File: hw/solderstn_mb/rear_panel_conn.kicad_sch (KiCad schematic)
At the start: 44 parts, among them J1001 SJ-3571N, J1002 Conn_WR-FAST_01x03, J1003 Conn_WR-FAST_01x03, J1004 PicoBlade_v4p_0533980471, J1005 PicoBlade_v4p_0533980471, J1006 USB_B-TE_1734346-1, J1007 IDC_2x5, J1008 USB_A-CUI-UJ2-AH-1-SMT, J1009 Molex_NanoFit-1x02, J1010 Conn_01x04, J1011 STX-3501-3N_(TTL-232R-xV-AJ), U1001 USBLC6-2SC6, U1002 74LVC2G17gw, U1003 USBLC6-2SC6

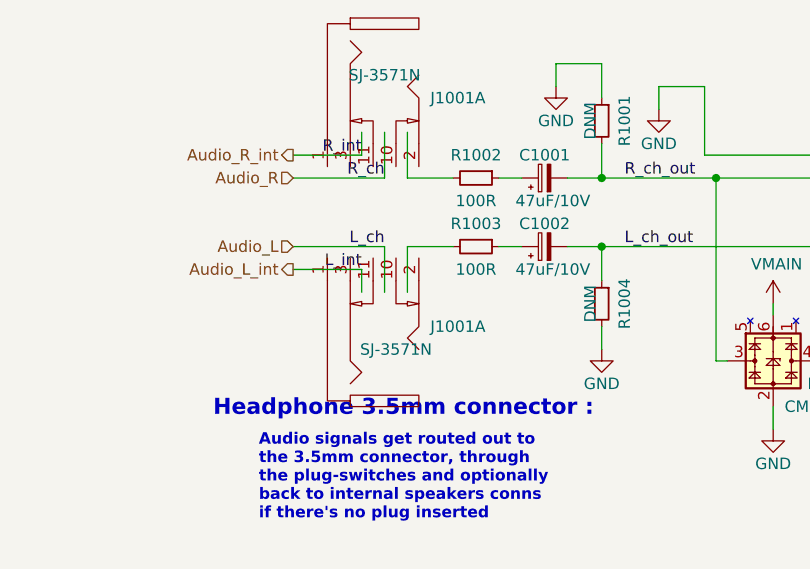
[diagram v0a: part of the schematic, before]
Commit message: Placeholder 3d-models for rear-panel (w. conns), PSU, Bottom-plate, front-panel (w. conns), outer fp
With these placeholder mech. objects, the build-in 3d view of MB pcb features most of the mechanical
objects that constrain components placements. So 3d-view can be used to quickly check and iterate
placements to avoid 3d collisions, without having to first export MB STEP into FreeCAD and muck around
only to have to repeat again for each iteration
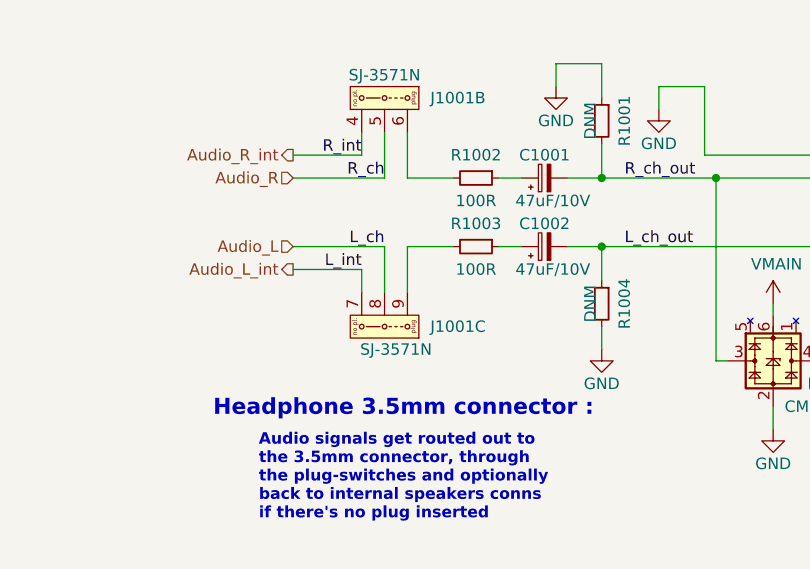
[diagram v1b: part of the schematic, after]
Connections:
- net Audio_L: now also J1001.8 (b)
- net Audio_L_int: now also J1001.7 (nc_b)
- net Audio_R: now also J1001.5 (a)
- net Audio_R_int: now also J1001.4 (nc_a)
- net at R1002.2: now also J1001.6 (no_a)
- net at R1003.2: now also J1001.9 (no_b)
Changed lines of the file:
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@@
     (pin "1")
   )
-  (symbol (lib_id "Device:R_Small") (at 204.47 31.75 270)
+  (symbol (lib_id "Device:R_Small") (at 204.47 31.75 270) (unit 1)
     (in_bom yes) (on_board yes)
     (property "Reference" "R1002" (id 0) (at 204.47 29.21 90))
@@
     (pin "2")
   )
-  (symbol (lib_id "Device:CP_Small") (at 212.09 31.75 90)
+  (symbol (lib_id "Device:CP_Small") (at 212.09 31.75 90) (unit 1)
     (in_bom yes) (on_board yes)
     (property "Reference" "C1001" (id 0) (at 212.09 29.21 90))
@@
     (pin "2")
   )
-  (symbol (lib_id "Device:R_Small") (at 204.47 39.37 270)
+  (symbol (lib_id "Device:R_Small") (at 204.47 39.37 270) (unit 1)
     (in_bom yes) (on_board yes)
     (property "Reference" "R1003" (id 0) (at 204.47 36.83 90))
@@
     (pin "2")
   )
-  (symbol (lib_id "Device:CP_Small") (at 212.09 39.37 90)
+  (symbol (lib_id "Device:CP_Small") (at 212.09 39.37 90) (unit 1)
     (in_bom yes) (on_board yes)
     (property "Reference" "C1002" (id 0) (at 212.09 36.83 90))
@@
     (pin "2")
   )
-  (symbol (lib_id "customlib_mj:SJ-3571N") (at 252.73 35.56 0) (mirror y)
+  (symbol (lib_id "customlib_mj:SJ-3571N") (at 252.73 35.56 0) (mirror y) (unit 1)
     (in_bom yes) (on_board yes)
     (property "Reference" "J1001" (id 0) (at 267.3604 33.6804 0))
@@
     (pin "3")
   )
-  (symbol (lib_id "power:GND") (at 224.79 24.13 0)
+  (symbol (lib_id "power:GND") (at 224.79 24.13 0) (unit 1)
     (in_bom yes) (on_board yes)
     (property "Reference" "#PWR01002" (id 0) (at 224.79 30.48 0)
@@
     (pin "1")
   )
-  (symbol (lib_id "customlib_mj:SJ-3571N") (at 194.31 22.86 90) (mirror x)
+  (symbol (lib_id "customlib_mj:SJ-3571N") (at 194.31 22.86 90) (mirror x) (unit 2)
     (in_bom yes) (on_board yes)
     (property "Reference" "J1001" (id 0) (at 199.39 22.86 90)
@@
     (pin "6")
   )
-  (symbol (lib_id "customlib_mj:SJ-3571N") (at 194.31 48.26 90)
+  (symbol (lib_id "customlib_mj:SJ-3571N") (at 194.31 48.26 90) (unit 3)
     (in_bom yes) (on_board yes)
     (property "Reference" "J1001" (id 0) (at 199.39 48.26 90)
@@
     (pin "1")
   )
-  (symbol (lib_id "Device:R_Small") (at 218.44 45.72 0) (mirror y)
+  (symbol (lib_id "Device:R_Small") (at 218.44 45.72 0) (mirror y) (unit 1)
     (in_bom yes) (on_board yes)
     (property "Reference" "R1004" (id 0) (at 220.98 45.72 90))
@@
     (pin "2")
   )
-  (symbol (lib_id "Device:R_Small") (at 218.44 25.4 0) (mirror y)
+  (symbol (lib_id "Device:R_Small") (at 218.44 25.4 0) (mirror y) (unit 1)
     (in_bom yes) (on_board yes)
     (property "Reference" "R1001" (id 0) (at 220.98 25.4 90))
